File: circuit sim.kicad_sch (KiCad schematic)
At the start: 3 parts

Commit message: changed stuff in circuit
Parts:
- added C1: 470nF, symbol Device:C
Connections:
- net at R2.1: now also C1.2; no longer R1.2
- new net: C1.1, R1.2
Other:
- moved on the sheet: R2

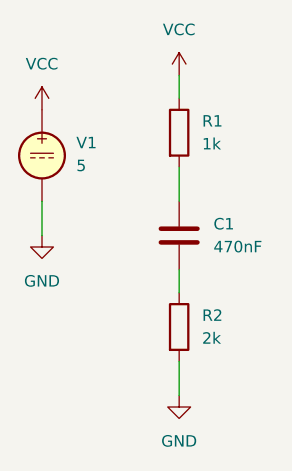
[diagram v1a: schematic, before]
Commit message: Added another tool
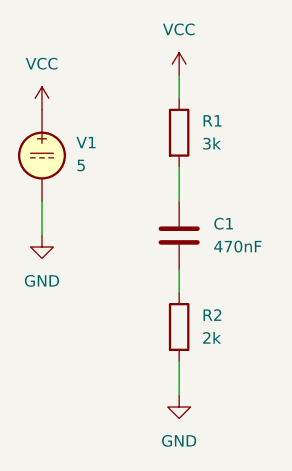
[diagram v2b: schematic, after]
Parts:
- R1: value 1k -> 3k
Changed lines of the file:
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@@
 		(fields_autoplaced yes)
 		(property "Reference" "R1"
-			(at 139.7 71.1199 0)
+			(at 139.7 71.12 0)
 			(effects
 				(font
@@
 			)
 		)
-		(property "Value" "1k"
-			(at 139.7 73.6599 0)
+		(property "Value" "3k"
+			(at 139.7 73.66 0)
 			(effects
 				(font
